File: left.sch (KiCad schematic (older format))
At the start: 92 parts, among them J1 Buzzer_magnetic, J11 Conn_01x01, J12 Conn_01x01, J13 Conn_01x01, J14 Conn_01x01, J15 Conn_01x01, J16 Conn_01x01, J17 Conn_01x01, J2 reset, J25 Buzzer_piezo, J3 ISP, J7 Conn_01x01, J9 UTC16-G, P3 WS2812, P4 SJ-43514-SMT, SW1 Socket, SW10 Socket, SW11 Socket, SW12 Socket, SW13 Socket, SW14 Socket, SW15 Socket, SW16 Socket, SW17 Socket, SW18 Socket, SW19 Socket, SW2 Socket, SW20 Socket, SW21 Socket, SW22 Socket, SW23 Socket, SW24 Socket, SW3 Socket, SW4 Socket, SW49 FSMSM, SW5 Socket, SW6 Socket, SW7 Socket, SW8 Socket, SW9 Socket, U1 ATMega32U4, Y1 16MHz

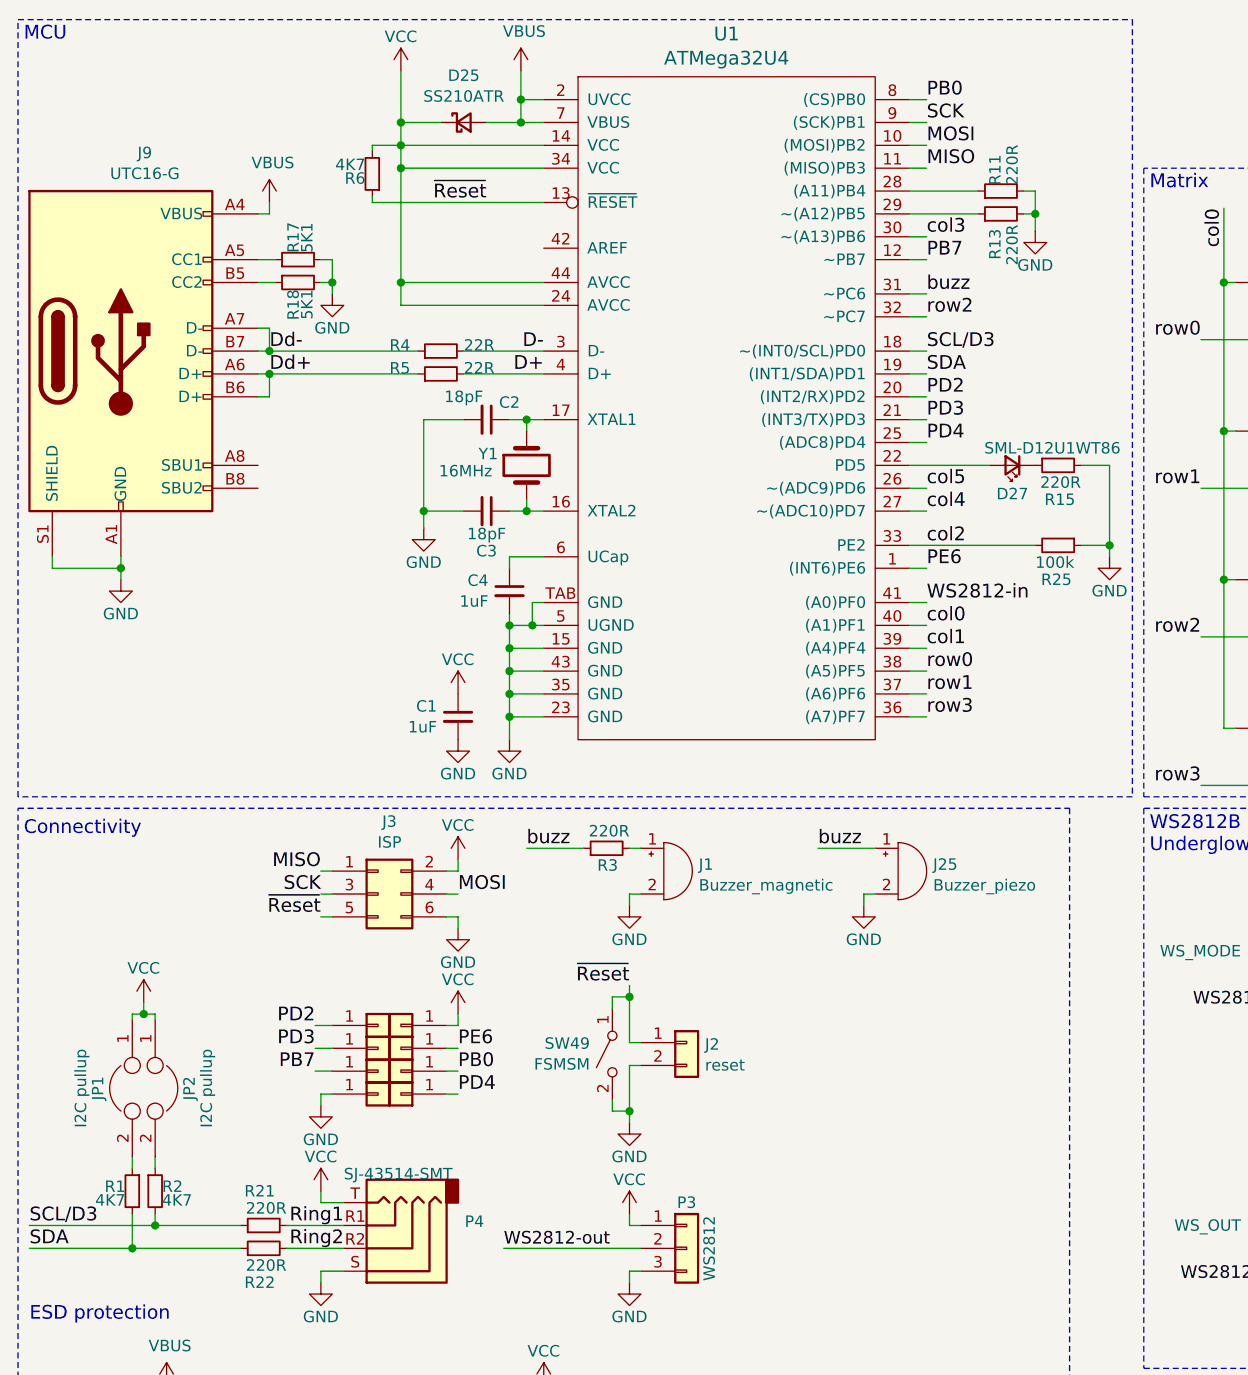
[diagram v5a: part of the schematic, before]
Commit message: Updated I2C pull-up values
Updated the values to ensure the effect of the newly added series resistors don't cause the low level to exceed chip specifications for i2c potentially leading to communication issues if using i2c
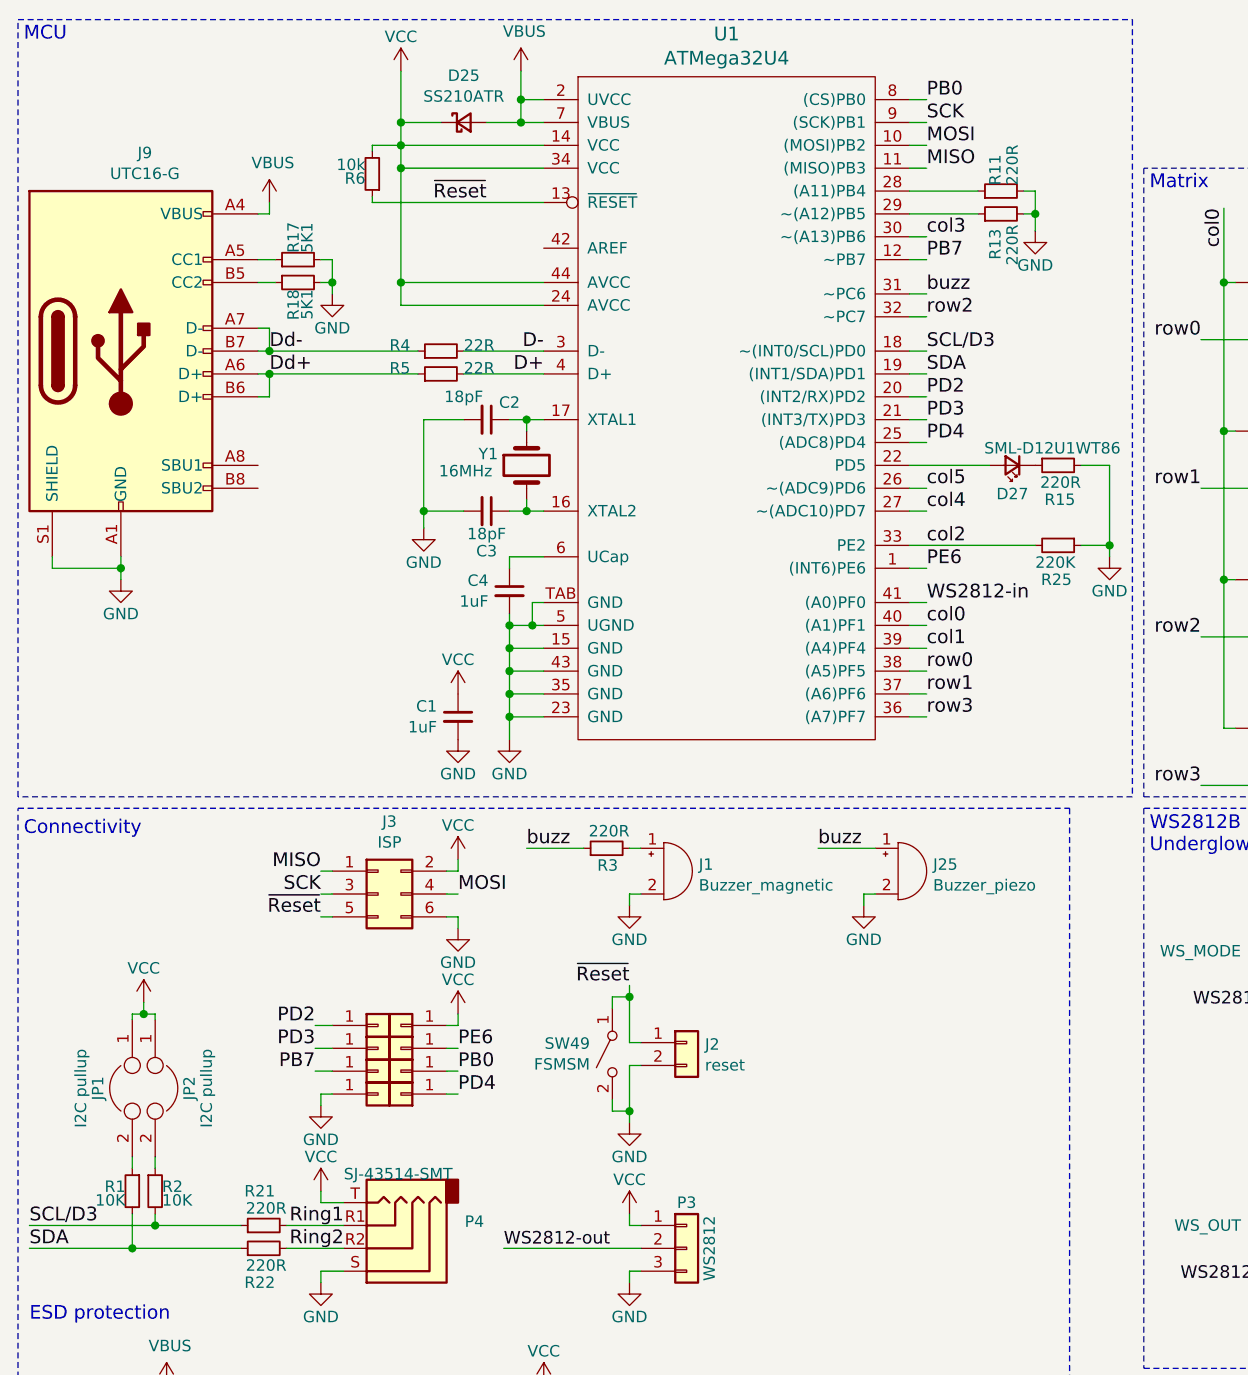
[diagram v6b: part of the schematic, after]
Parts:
- R1, R2: value 4K7 -> 10K
- R25: value 100k -> 220K
- R6: value 4K7 -> 10k
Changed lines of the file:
@@
 P 1425 5675
 F 0 "R2" H 1455 5695 50  0000 L CNN
-F 1 "4K7" H 1455 5635 50  0000 L CNN
+F 1 "10K" H 1455 5635 50  0000 L CNN
 F 2 "Resistor_SMD:R_0603_1608Metric" H 1425 5675 50  0001 C CNN
 F 3 "" H 1425 5675 50  0000 C CNN
@@
 P 1325 5675
 F 0 "R1" H 1355 5695 50  0000 L CNN
-F 1 "4K7" H 1355 5635 50  0000 L CNN
+F 1 "10K" H 1355 5635 50  0000 L CNN
 F 2 "Resistor_SMD:R_0603_1608Metric" H 1325 5675 50  0001 C CNN
 F 3 "" H 1325 5675 50  0000 C CNN
@@
 P 2375 1225
 F 0 "R6" H 2405 1245 50  0000 L CNN
-F 1 "4K7" H 2405 1185 50  0000 L CNN
+F 1 "10k" H 2405 1185 50  0000 L CNN
 F 2 "Resistor_SMD:R_0603_1608Metric" H 2375 1225 50  0001 C CNN
 F 3 "" H 2375 1225 50  0000 C CNN
@@
 P 5375 2850
 F 0 "R25" V 5525 2775 50  0000 L CNN
-F 1 "100k" V 5450 2750 50  0000 L CNN
+F 1 "220K" V 5450 2750 50  0000 L CNN
 F 2 "Resistor_SMD:R_0603_1608Metric" H 5375 2850 50  0001 C CNN
 F 3 "" H 5375 2850 50  0000 C CNN
